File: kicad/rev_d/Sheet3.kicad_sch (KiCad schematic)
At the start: 94 parts, among them U1 74HCT1G04, X10 ST-214C, X14 AAFP/AC97 audio, X16 PLB1-4I, X17 PLB1-4I, X18 PLB1-4I, X20 PLB1-4I

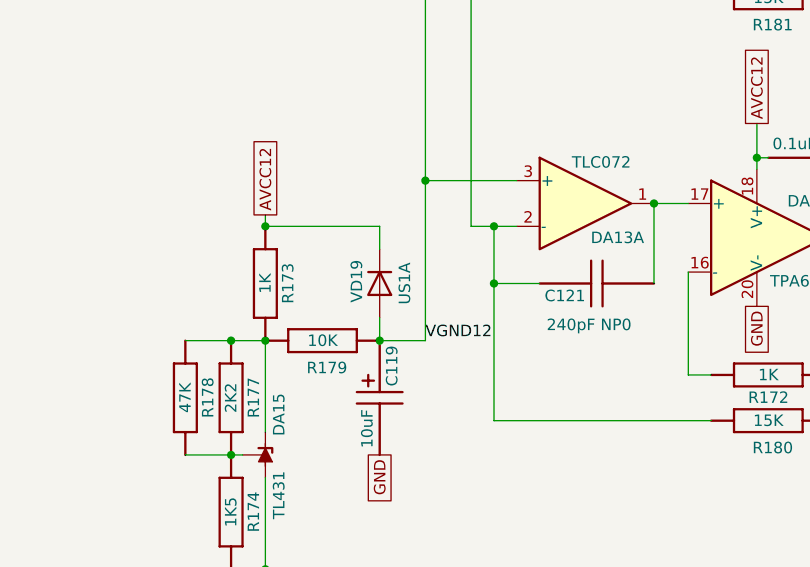
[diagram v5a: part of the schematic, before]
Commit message: pentevo: add datasheets for SS14 and S1A diodes; rev. D: replace linear regulator diodes with S1A
git-svn-id: svn://localhost/local-pentevo@1223 c6c76956-fad2-4150-a3a9-ea0a427205ba
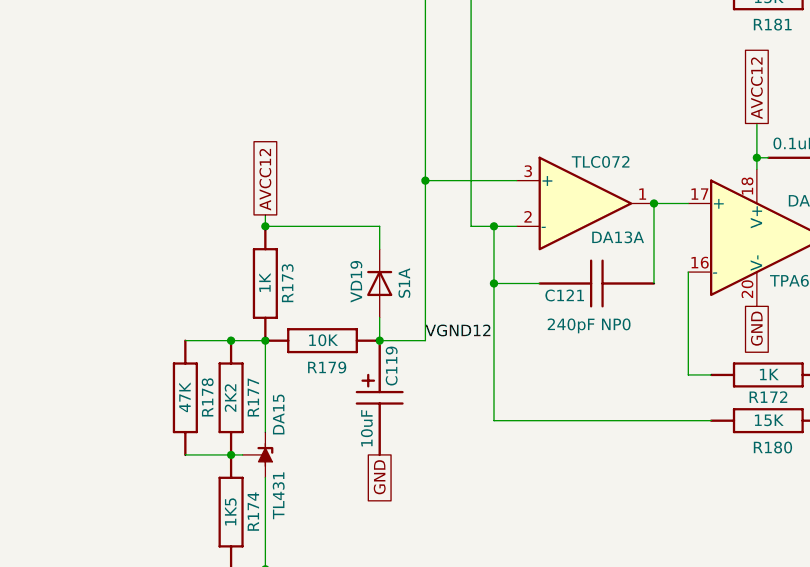
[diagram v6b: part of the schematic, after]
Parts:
- VD19: value US1A -> S1A
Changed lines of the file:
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@@
 			)
 		)
-		(property "Value" "US1A"
+		(property "Value" "S1A"
 			(at 188.214 224.79 0)
 			(effects

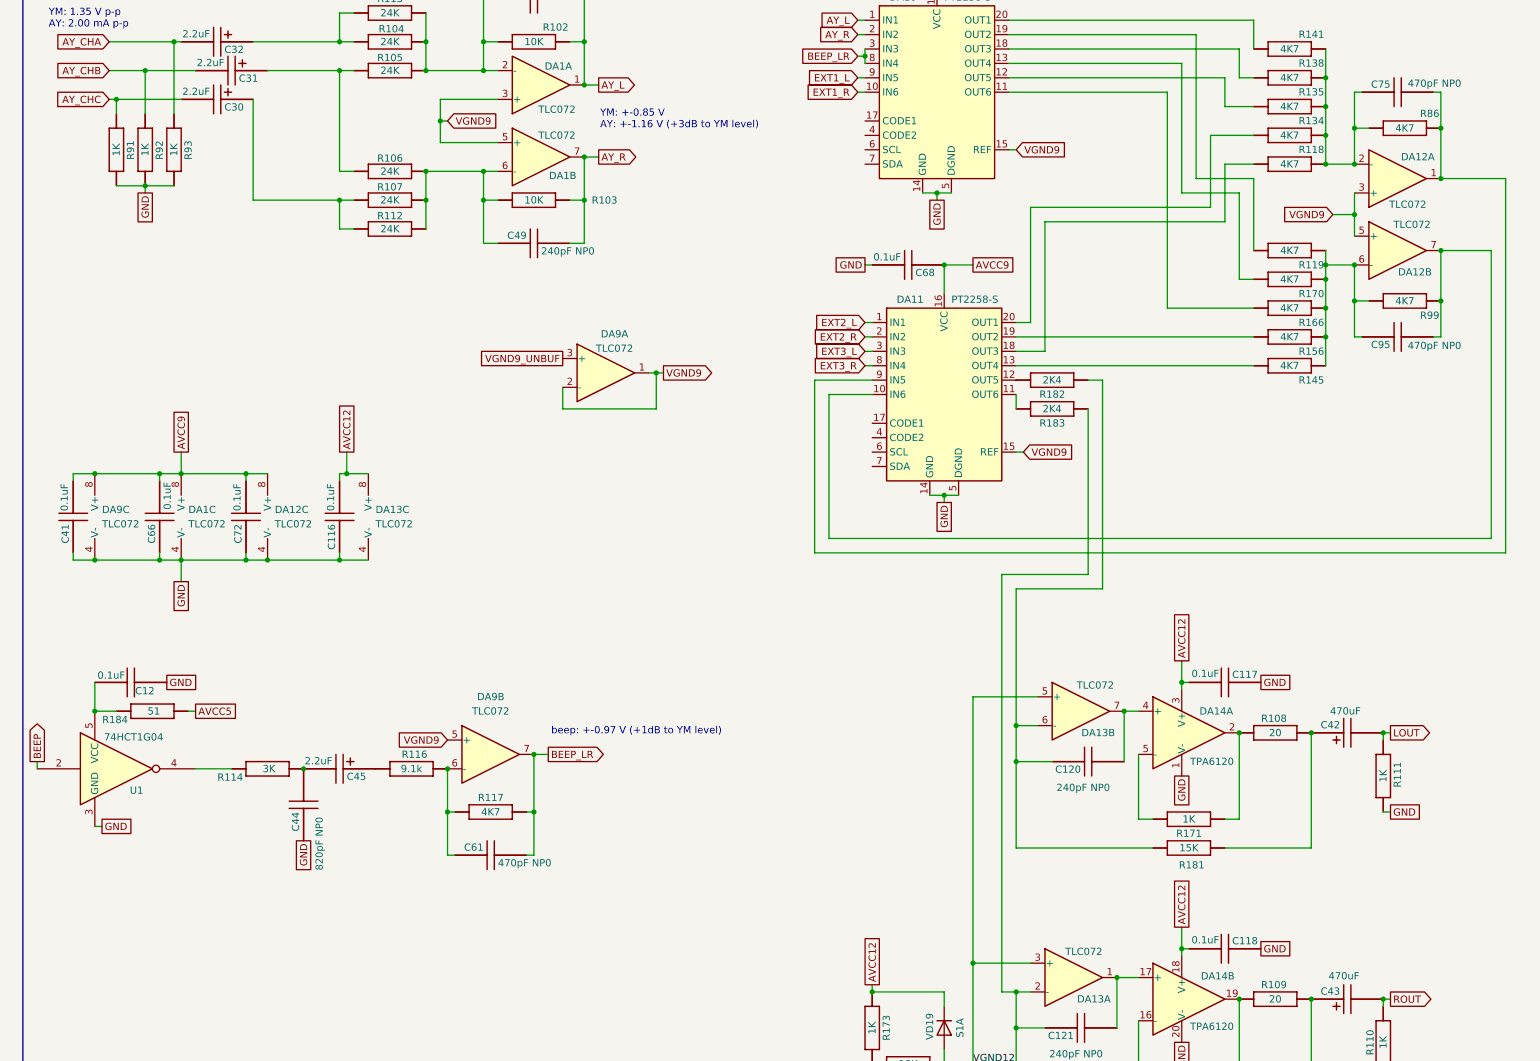
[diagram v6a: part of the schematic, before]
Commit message: pentevo: rev D: replace tlc072 with tlv9162; replace m29f040b to m29f032d; TODO: add pca9555 to control high address pins of flash ic
git-svn-id: svn://localhost/local-pentevo@1227 c6c76956-fad2-4150-a3a9-ea0a427205ba
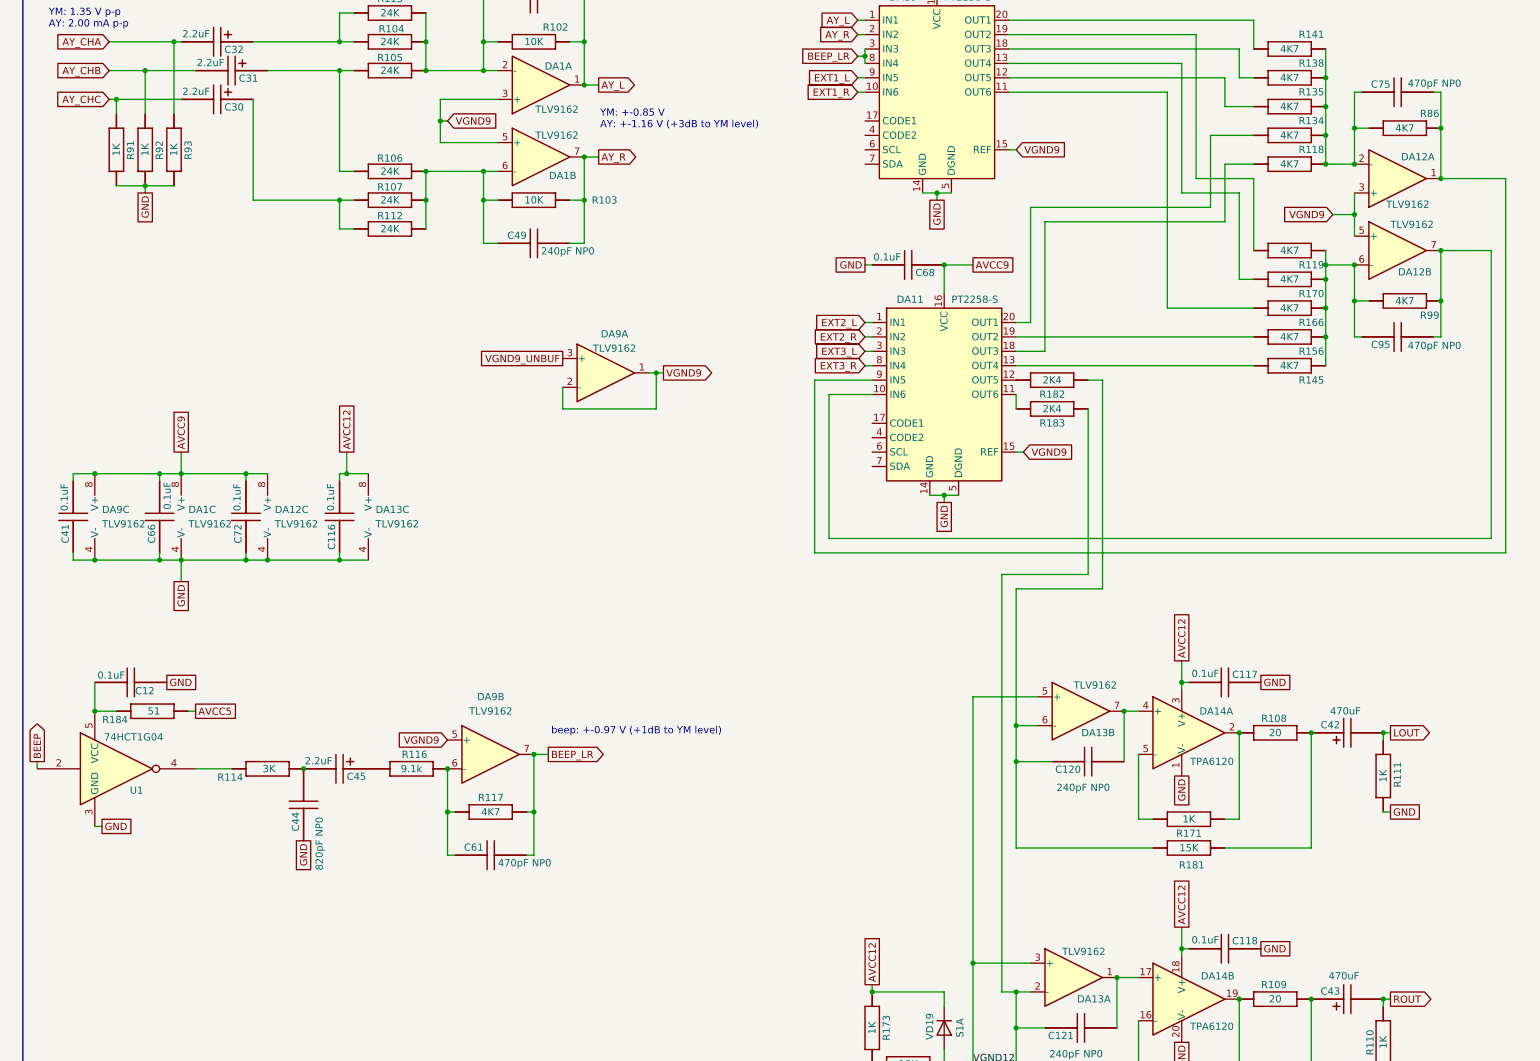
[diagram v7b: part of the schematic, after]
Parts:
- DA1, DA12, DA13, DA9: value TLC072 -> TLV9162
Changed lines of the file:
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@@
 			)
 		)
-		(property "Value" "TLC072"
+		(property "Value" "TLV9162"
 			(at 267.97 83.058 0)
 			(effects
@@
 			)
 		)
-		(property "Value" "TLC072"
+		(property "Value" "TLV9162"
 			(at 267.208 79.502 0)
 			(effects
@@
 			)
 		)
-		(property "Value" "TLC072"
+		(property "Value" "TLV9162"
 			(at 212.09 164.338 0)
 			(effects
@@
 			)
 		)
-		(property "Value" "TLC072"
+		(property "Value" "TLV9162"
 			(at 117.094 62.738 0)
 			(effects
@@
 			)
 		)
-		(property "Value" "TLC072"
+		(property "Value" "TLV9162"
 			(at 117.094 67.31 0)
 			(effects
@@
 			)
 		)
-		(property "Value" "TLC072"
+		(property "Value" "TLV9162"
 			(at 85.09 135.8899 0)
 			(effects
@@
 			)
 		)
-		(property "Value" "TLC072"
+		(property "Value" "TLV9162"
 			(at 67.31 135.8899 0)
 			(effects
@@
 			)
 		)
-		(property "Value" "TLC072"
+		(property "Value" "TLV9162"
 			(at 52.07 135.8899 0)
 			(effects
@@
 			)
 		)
-		(property "Value" "TLC072"
+		(property "Value" "TLV9162"
 			(at 127.254 104.902 0)
 			(effects
@@
 			)
 		)
-		(property "Value" "TLC072"
+		(property "Value" "TLV9162"
 			(at 210.058 211.328 0)
 			(effects
@@
 			)
 		)
-		(property "Value" "TLC072"
+		(property "Value" "TLV9162"
 			(at 36.83 135.8899 0)
 			(effects
@@
 			)
 		)
-		(property "Value" "TLC072"
+		(property "Value" "TLV9162"
 			(at 105.41 168.91 0)
 			(effects

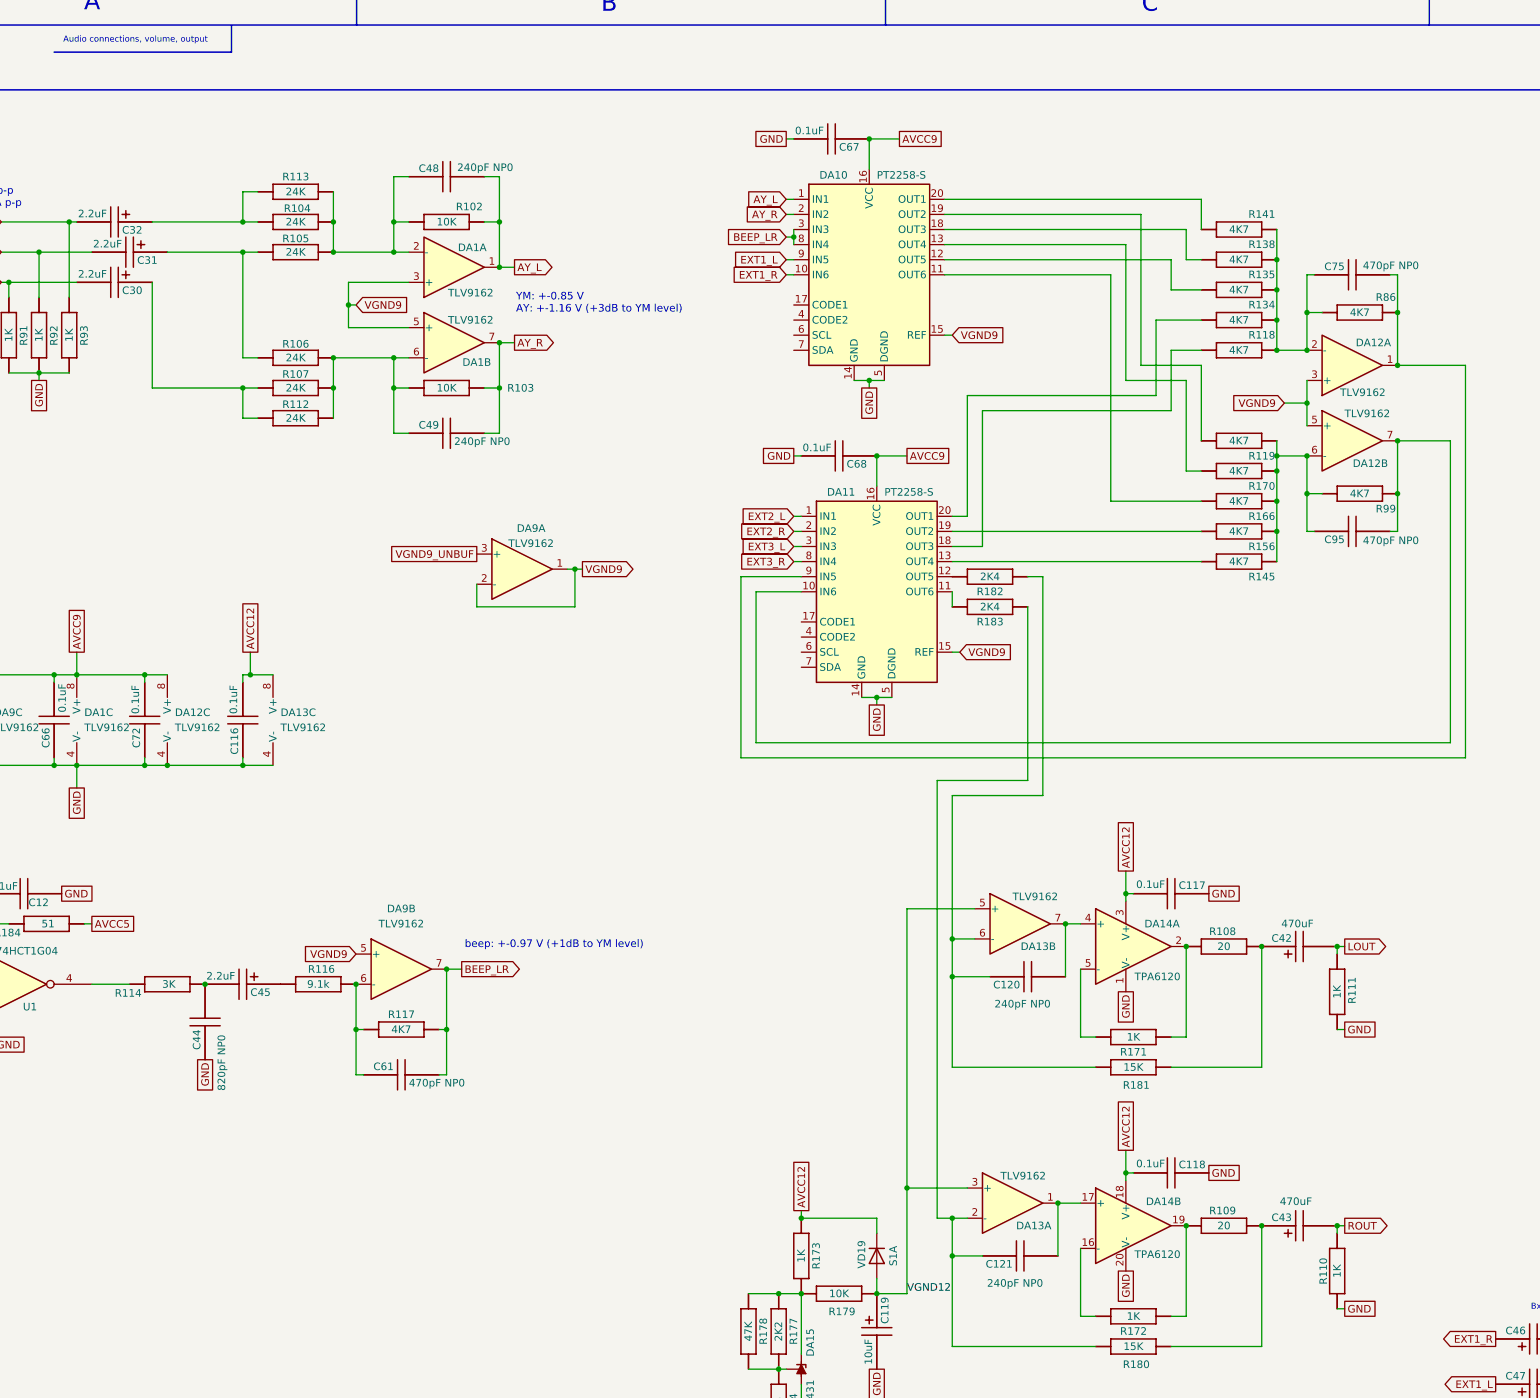
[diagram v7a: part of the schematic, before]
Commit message: pentevo: rev D: implemented lopass 30kHz filter, with a model
git-svn-id: svn://localhost/local-pentevo@1239 c6c76956-fad2-4150-a3a9-ea0a427205ba
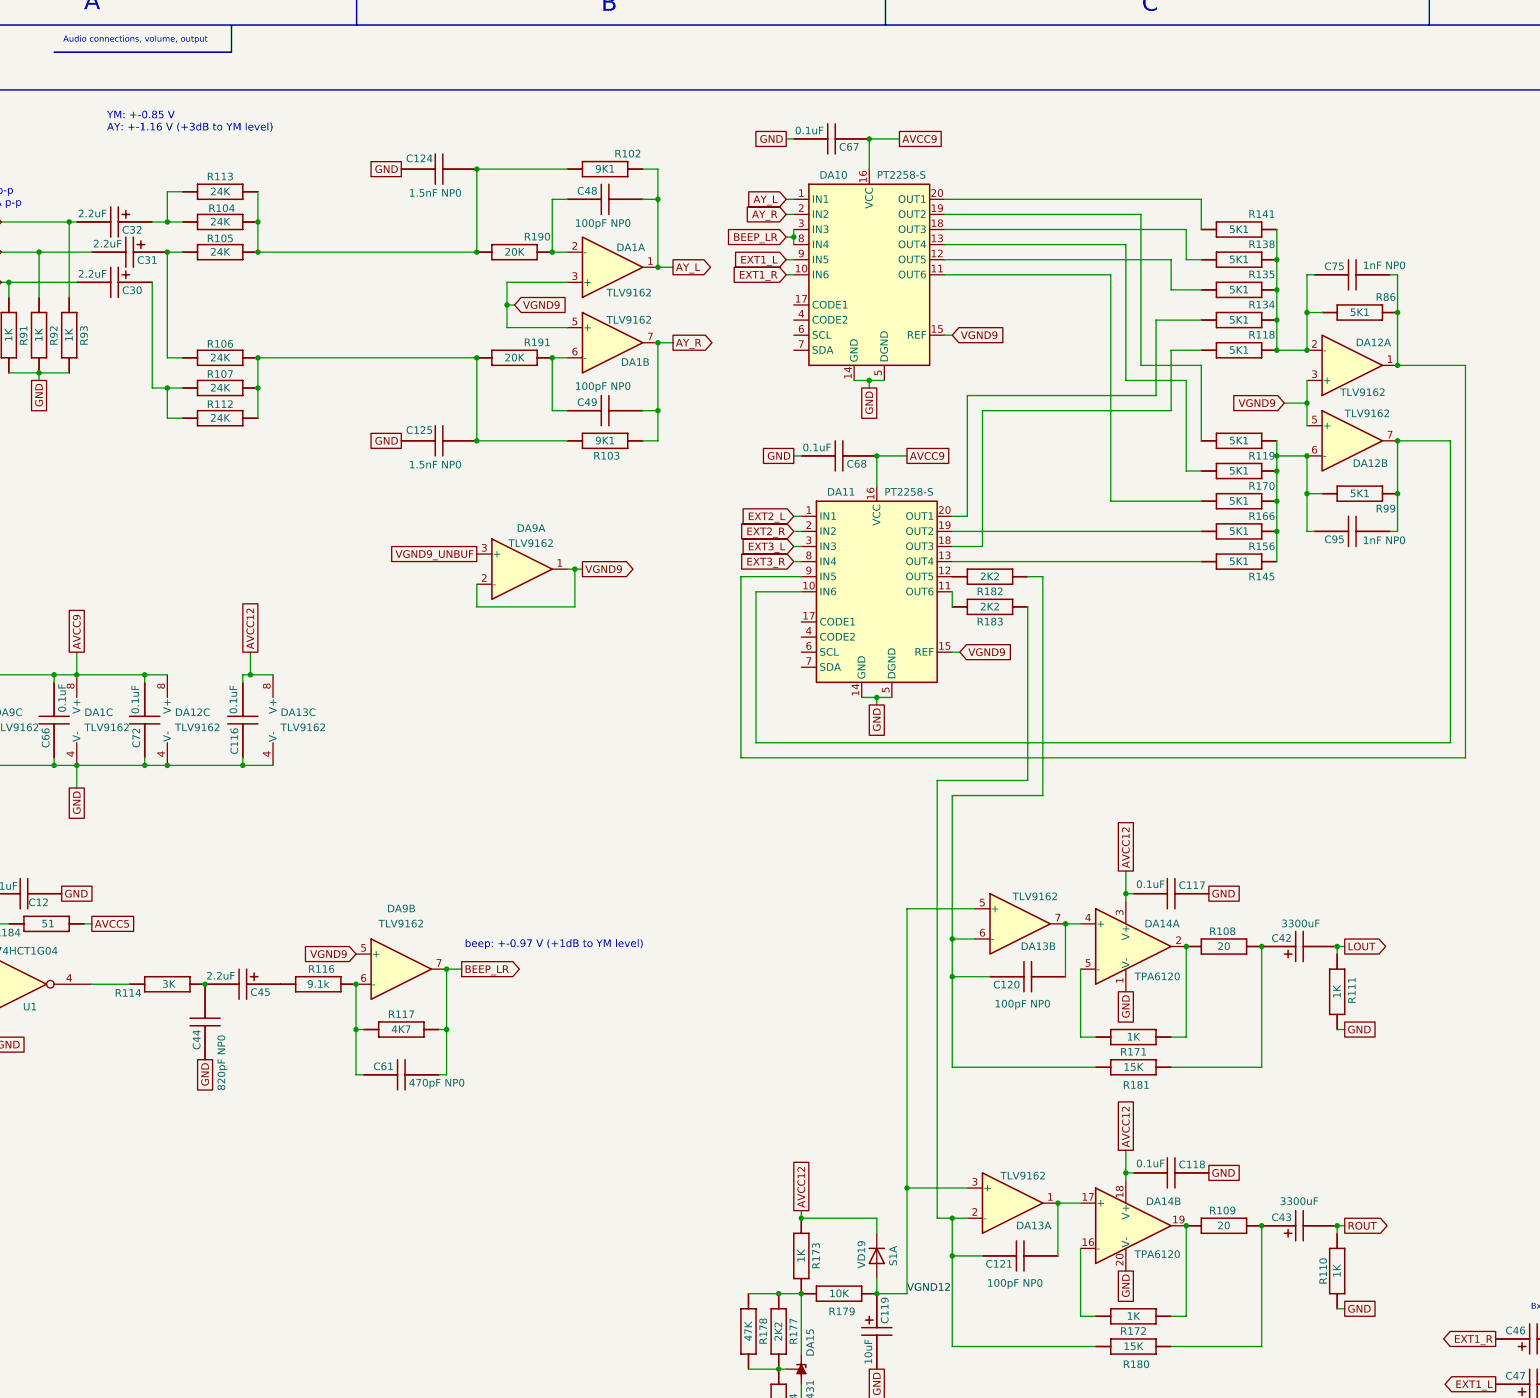
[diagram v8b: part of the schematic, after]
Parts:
- added C124, C125: 1.5nF NP0, C-CHIP, symbol eva-altium-import:Sheet2_0_CAPCHIP
- added R190, R191: 20K, R-CHIP, symbol eva-altium-import:Sheet2_2_mirrored_RESCHIP
- C120, C121, C48, C49: value 240pF NP0 -> 100pF NP0
- C42, C43: value 470uF -> 3300uF
- C75, C95: value 470pF NP0 -> 1nF NP0
- R102, R103: value 10K -> 9K1
- R118, R119, R134, R135, R138, R141, R145, R156, R166, R170, R86, R99: value 4K7 -> 5K1
- R182, R183: value 2K4 -> 2K2
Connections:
- net GND: now also C124.1, C125.1
- net at R103.2 (i/o1), R106.1 (i/o), R107.1 (i/o)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: now also C125.2, R191.2 (i/o1); no longer C49.1, DA1.6 (-)
- net at R102.2 (i/o1), R104.1 (i/o), R105.1 (i/o)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: now also C124.2, R190.2 (i/o1); no longer C48.1, DA1.2 (-)
- new net: C48.1, DA1.2 (-), R190.1 (i/o)
- new net: C49.1, DA1.6 (-), R191.1 (i/o)
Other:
- moved on the sheet: C48, C49, DA1A, DA1B, R102, R103, R104, R105, R106, R107, R112, R113
